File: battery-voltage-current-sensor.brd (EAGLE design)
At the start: 100 x 100 mm, 66 parts, among them IC1 ACS758LCB-050B-PFF-T, IC3 ADS1115IDGST, J1 B4B-XH-A(LF)(SN), T1 C8545, T2 C8545, T3 C8545

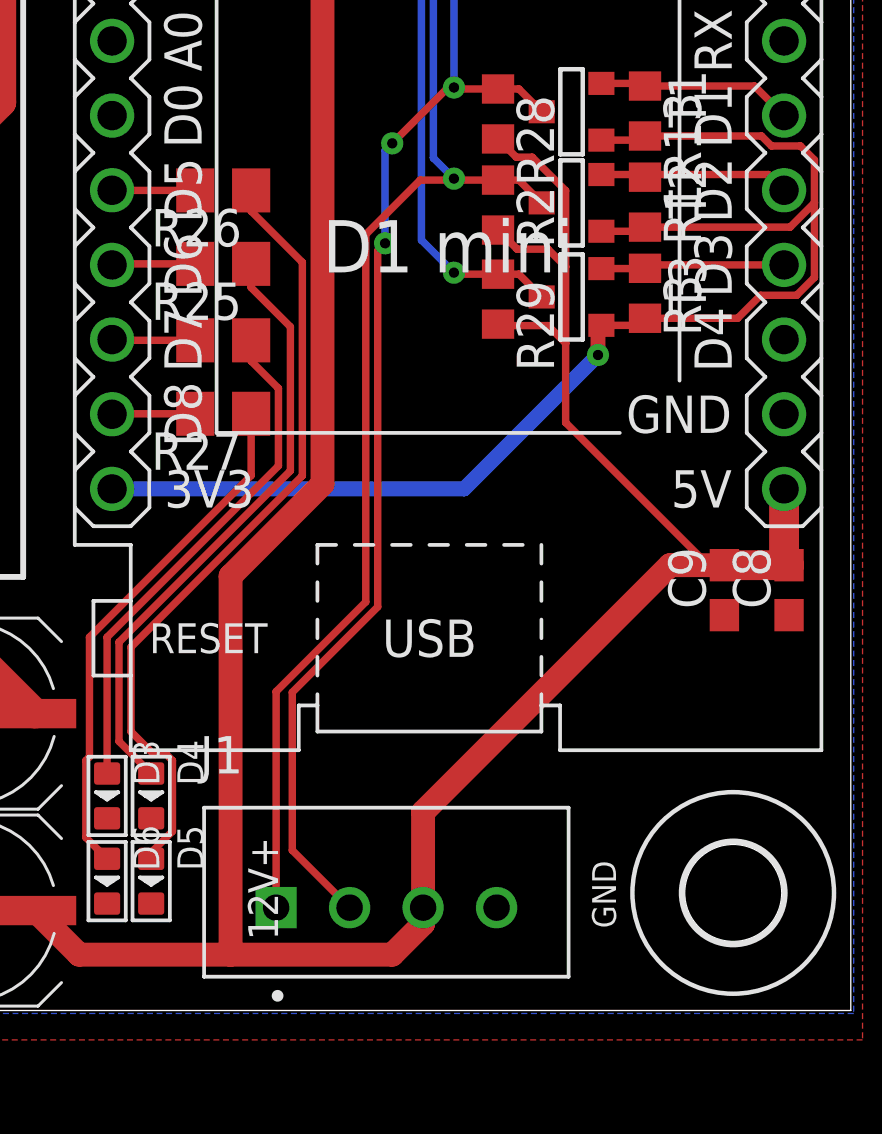
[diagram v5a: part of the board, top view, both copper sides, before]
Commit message: connector rotated, ready to manufacture, ordered
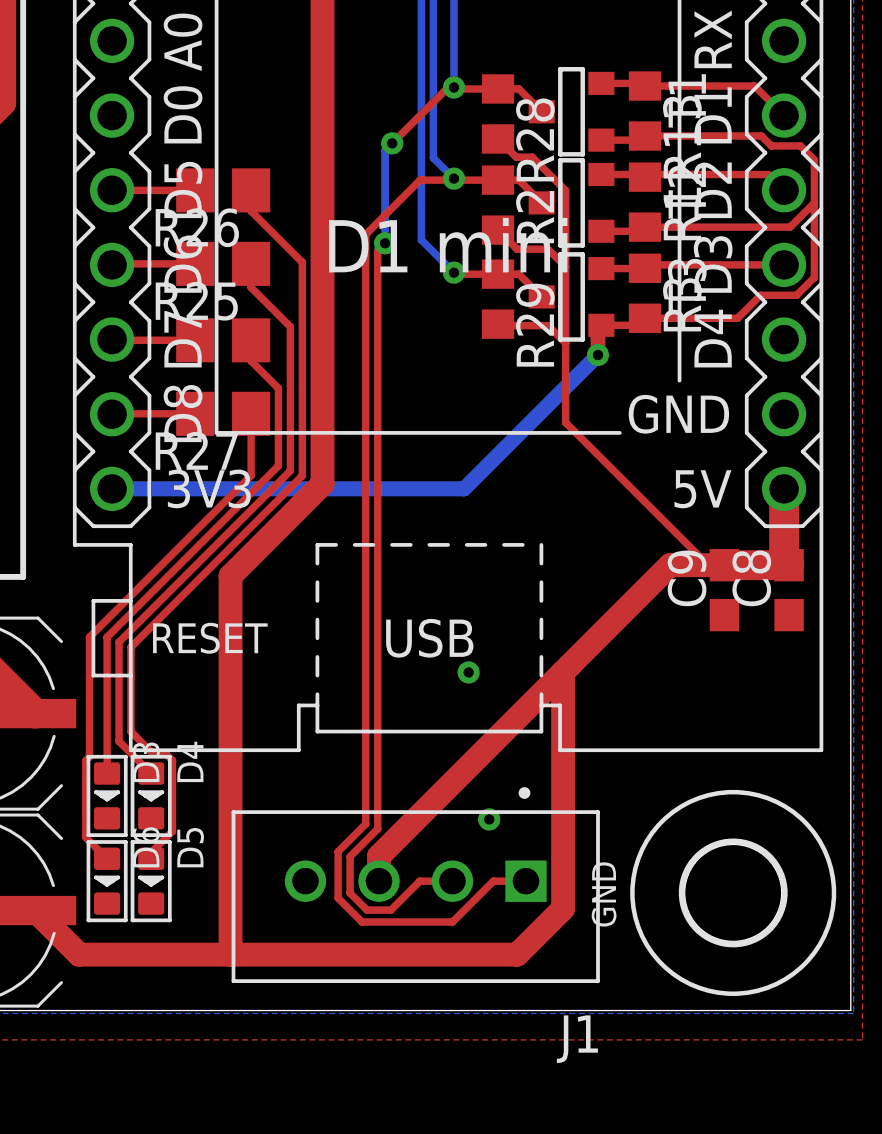
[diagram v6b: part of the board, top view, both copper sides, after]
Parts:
- moved J1 1.35 mm to (85.2, 4.40), turned to 180 degrees
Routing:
- net +5V/1: track 205.0 -> 217.2 mm
- net SDA: track 104.6 -> 110.7 mm
- net SCL: track 105.3 -> 107.3 mm
- net GND: vias 0 -> 2
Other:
- board text removed: "12V+"
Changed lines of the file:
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@@
 <text x="31.6" y="97" size="1.778" layer="25">Battery</text>
 <text x="30.4" y="2.8" size="1.778" layer="25">Output</text>
-<text x="79.5" y="5.9" size="1.016" layer="25" rot="R270">12V+</text>
 <text x="91.2" y="5.1" size="0.8128" layer="25" rot="R270">GND</text>
 </plain>
@@
 <element name="C2" library="rcl" library_urn="urn:adsk.eagle:library:334" package="UD-6,3X7,7_NICHICON" package3d_urn="urn:adsk.eagle:package:23472/1" value="C473426" x="69.9" y="3.4" smashed="yes">
 <attribute name="NAME" x="66.725" y="7.21" size="1.016" layer="25"/>
-<attribute name="VALUE" x="66.725" y="-1.045" size="1.016" layer="27"/>
 </element>
 <element name="C3" library="rcl" library_urn="urn:adsk.eagle:library:334" package="C0603" package3d_urn="urn:adsk.eagle:package:23616/2" value="100nF" x="95.9" y="82.5" smashed="yes" rot="R270">
@@
 <element name="C8" library="rcl" library_urn="urn:adsk.eagle:library:334" package="C0603" package3d_urn="urn:adsk.eagle:package:23616/2" value="100nF" x="97.9" y="14.3" smashed="yes" rot="R90">
 <attribute name="NAME" x="97.265" y="13.665" size="1.27" layer="25" rot="R90"/>
-<attribute name="VALUE" x="99.805" y="13.665" size="1.27" layer="27" rot="R90"/>
 </element>
 <element name="C9" library="rcl" library_urn="urn:adsk.eagle:library:334" package="C0603" package3d_urn="urn:adsk.eagle:package:23616/2" value="100nF" x="95.7" y="14.3" smashed="yes" rot="R90">
@@
 <attribute name="VALUE" x="86.095" y="24.835" size="1.27" layer="27" rot="R270"/>
 </element>
-<element name="J1" library="Headers" library_urn="urn:adsk.eagle:library:11687645" package="B4B-XH-A(LF)(SN)" package3d_urn="urn:adsk.eagle:package:19181368/7" value="B4B-XH-A(LF)(SN)" x="84.2" y="3.5" smashed="yes">
-<attribute name="CREATED_BY" value="PCBLayout.com" x="84.2" y="3.5" size="1.778" layer="27" display="off"/>
-<attribute name="DIGIKEY_PARTNO" value="455-2249-ND" x="84.2" y="3.5" size="1.778" layer="27" display="off"/>
-<attribute name="MANUFACTURER" value="JST Sales America Inc." x="84.2" y="3.5" size="1.778" layer="27" display="off"/>
-<attribute name="MPN" value="B4B-XH-A(LF)(SN)" x="84.2" y="3.5" size="1.778" layer="27" display="off"/>
-<attribute name="NAME" x="77.857" y="8.065" size="1.27" layer="25"/>
-<attribute name="VALUE" x="77.596" y="-1.199" size="1.27" layer="27"/>
+<element name="J1" library="Headers" library_urn="urn:adsk.eagle:library:11687645" package="B4B-XH-A(LF)(SN)" package3d_urn="urn:adsk.eagle:package:19181368/7" value="B4B-XH-A(LF)(SN)" x="85.2" y="4.4" smashed="yes" rot="R180">
+<attribute name="CREATED_BY" value="PCBLayout.com" x="85.2" y="4.4" size="1.778" layer="27" rot="R180" display="off"/>
+<attribute name="DIGIKEY_PARTNO" value="455-2249-ND" x="85.2" y="4.4" size="1.778" layer="27" rot="R180" display="off"/>
+<attribute name="MANUFACTURER" value="JST Sales America Inc." x="85.2" y="4.4" size="1.778" layer="27" rot="R180" display="off"/>
+<attribute name="MPN" value="B4B-XH-A(LF)(SN)" x="85.2" y="4.4" size="1.778" layer="27" rot="R180" display="off"/>
+<attribute name="NAME" x="91.543" y="-0.165" size="1.27" layer="25" rot="R180"/>
 </element>
 </elements>
@@
 <wire x1="68.2" y1="51" x2="67.89" y2="50.69" width="0.1524" layer="1"/>
 <contactref element="J1" pad="4"/>
+<via x="87" y="11.5" extent="1-16" drill="0.35"/>
+<via x="87.7" y="6.5" extent="1-16" drill="0.35"/>
 </signal>
 <signal name="+5V/1">
@@
 <wire x1="72.25" y1="3.4" x2="73.75" y2="1.9" width="0.8128" layer="1"/>
 <wire x1="73.75" y1="1.9" x2="78.9" y2="1.9" width="0.8128" layer="1"/>
-<wire x1="84.4" y1="1.9" x2="78.9" y2="1.9" width="0.8128" layer="1"/>
-<wire x1="84.4" y1="1.9" x2="85.45" y2="2.95" width="0.8128" layer="1"/>
-<wire x1="85.45" y1="2.95" x2="85.45" y2="3.5" width="0.8128" layer="1"/>
-<wire x1="85.45" y1="3.5" x2="85.45" y2="6.75" width="0.8128" layer="1"/>
 <wire x1="93.85" y1="15.15" x2="95.7" y2="15.15" width="0.8128" layer="1"/>
-<wire x1="85.45" y1="6.75" x2="93.85" y2="15.15" width="0.8128" layer="1"/>
 <wire x1="88" y1="29.65" x2="88.6206" y2="29.0294" width="0.254" layer="1"/>
 <wire x1="88.6206" y1="29.0294" x2="89.16253125" y2="29.0294" width="0.254" layer="1"/>
@@
 <wire x1="90.3" y1="20" x2="95.15" y2="15.15" width="0.254" layer="1"/>
 <wire x1="95.15" y1="15.15" x2="95.7" y2="15.15" width="0.254" layer="1"/>
-<wire x1="78.9" y1="1.9" x2="78.9" y2="14.78065625" width="0.8128" layer="1"/>
+<wire x1="78.9" y1="14.78065625" x2="78.9" y2="1.9" width="0.8128" layer="1"/>
 <wire x1="78.9" y1="14.78065625" x2="82.028" y2="17.90865625" width="0.8128" layer="1"/>
 <wire x1="82.028" y1="17.90865625" x2="82.028" y2="37.928" width="0.8128" layer="1"/>
 <wire x1="82.028" y1="37.928" x2="91.1" y2="47" width="0.8128" layer="1"/>
+<wire x1="83.95" y1="4.4" x2="83.95" y2="5.25" width="0.8128" layer="1"/>
+<wire x1="83.95" y1="5.25" x2="90.2128" y2="11.5128" width="0.8128" layer="1"/>
+<wire x1="90.45" y1="11.75" x2="93.85" y2="15.15" width="0.8128" layer="1"/>
+<wire x1="78.9" y1="1.9" x2="88.6482625" y2="1.9" width="0.8128" layer="1"/>
+<wire x1="88.6482625" y1="1.9" x2="90.2128" y2="3.4645375" width="0.8128" layer="1"/>
+<wire x1="90.2128" y1="11.5128" x2="90.45" y2="11.75" width="0.8128" layer="1"/>
+<wire x1="90.2128" y1="3.4645375" x2="90.2128" y2="11.5128" width="0.8128" layer="1"/>
 </signal>
 <signal name="SCL">
@@
 <wire x1="78.8" y1="96.5" x2="78.8" y2="96.2" width="0.254" layer="1"/>
 <contactref element="J1" pad="2"/>
-<wire x1="82.95" y1="3.5" x2="81" y2="5.45" width="0.254" layer="1"/>
-<wire x1="81" y1="5.45" x2="81" y2="10.8252625" width="0.254" layer="1"/>
-<wire x1="81" y1="10.8252625" x2="83.9064" y2="13.7316625" width="0.254" layer="1"/>
-<wire x1="83.9064" y1="25.8488" x2="84.1576" y2="26.1" width="0.254" layer="1"/>
+<wire x1="84.1576" y1="26.1" x2="83.9064" y2="25.8488" width="0.254" layer="1"/>
 <via x="84.1576" y="26.1" extent="1-16" drill="0.35"/>
 <wire x1="84.1576" y1="26.1" x2="84.1576" y2="29.2576" width="0.254" layer="16"/>
@@
 <wire x1="84.4" y1="29.5" x2="86.25" y2="31.35" width="0.254" layer="1"/>
 <wire x1="86.25" y1="31.35" x2="86.55" y2="31.35" width="0.254" layer="1"/>
-<wire x1="83.9064" y1="13.7316625" x2="83.9064" y2="25.8488" width="0.254" layer="1"/>
+<wire x1="82.9666" y1="3.99265625" x2="83.54265625" y2="3.4166" width="0.254" layer="1"/>
+<wire x1="83.54265625" y1="3.4166" x2="84.35734375" y2="3.4166" width="0.254" layer="1"/>
+<wire x1="83.9064" y1="6.17626875" x2="82.9666" y2="5.23646875" width="0.254" layer="1"/>
+<wire x1="82.9666" y1="5.23646875" x2="82.9666" y2="3.99265625" width="0.254" layer="1"/>
+<wire x1="84.35734375" y1="3.4166" x2="85.34074375" y2="4.4" width="0.254" layer="1"/>
+<wire x1="85.34074375" y1="4.4" x2="86.45" y2="4.4" width="0.254" layer="1"/>
+<wire x1="83.9064" y1="25.8488" x2="83.9064" y2="6.17626875" width="0.254" layer="1"/>
 </signal>
 <signal name="AIN0">
@@
 <wire x1="78.78500625" y1="95.71499375" x2="78.8" y2="95.7" width="0.254" layer="1"/>
 <contactref element="J1" pad="1"/>
-<wire x1="80.45" y1="3.5" x2="80.45" y2="10.85" width="0.254" layer="1"/>
-<wire x1="80.45" y1="10.85" x2="83.5" y2="13.9" width="0.254" layer="1"/>
-<wire x1="83.5" y1="13.9" x2="83.5" y2="26.4" width="0.254" layer="1"/>
-<wire x1="83.5" y1="26.4" x2="85.35" y2="28.25" width="0.254" layer="1"/>
+<wire x1="85.35" y1="28.25" x2="83.5" y2="26.4" width="0.254" layer="1"/>
 <wire x1="85.35" y1="28.25" x2="86.55" y2="28.25" width="0.254" layer="1"/>
+<wire x1="83.5" y1="6.34460625" x2="82.5602" y2="5.40480625" width="0.254" layer="1"/>
+<wire x1="82.5602" y1="5.40480625" x2="82.5602" y2="3.82431875" width="0.254" layer="1"/>
+<wire x1="82.5602" y1="3.82431875" x2="83.37431875" y2="3.0102" width="0.254" layer="1"/>
+<wire x1="83.37431875" y1="3.0102" x2="86.45094375" y2="3.0102" width="0.254" layer="1"/>
+<wire x1="86.45094375" y1="3.0102" x2="87.84074375" y2="4.4" width="0.254" layer="1"/>
+<wire x1="87.84074375" y1="4.4" x2="88.95" y2="4.4" width="0.254" layer="1"/>
+<wire x1="83.5" y1="26.4" x2="83.5" y2="6.34460625" width="0.254" layer="1"/>
 </signal>
 <signal name="ALERT">
